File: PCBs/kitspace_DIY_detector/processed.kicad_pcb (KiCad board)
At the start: 2 copper layers, 75 x 26 mm, 35 parts, among them J1 Conn_01x02_Female, J2 Conn_01x02_Female, U1 TLE2072

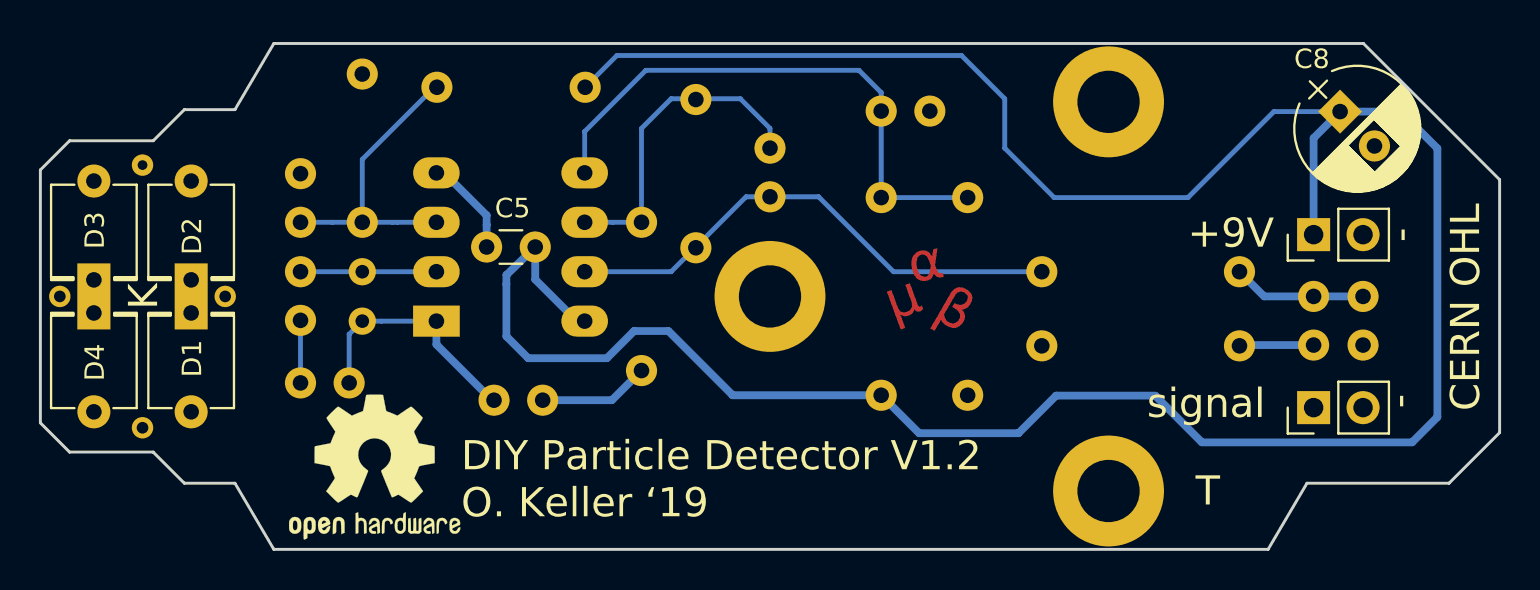
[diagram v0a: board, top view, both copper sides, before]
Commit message: recheck all circuits and clean up fill zone by rerouting the nets using freerouting and manually
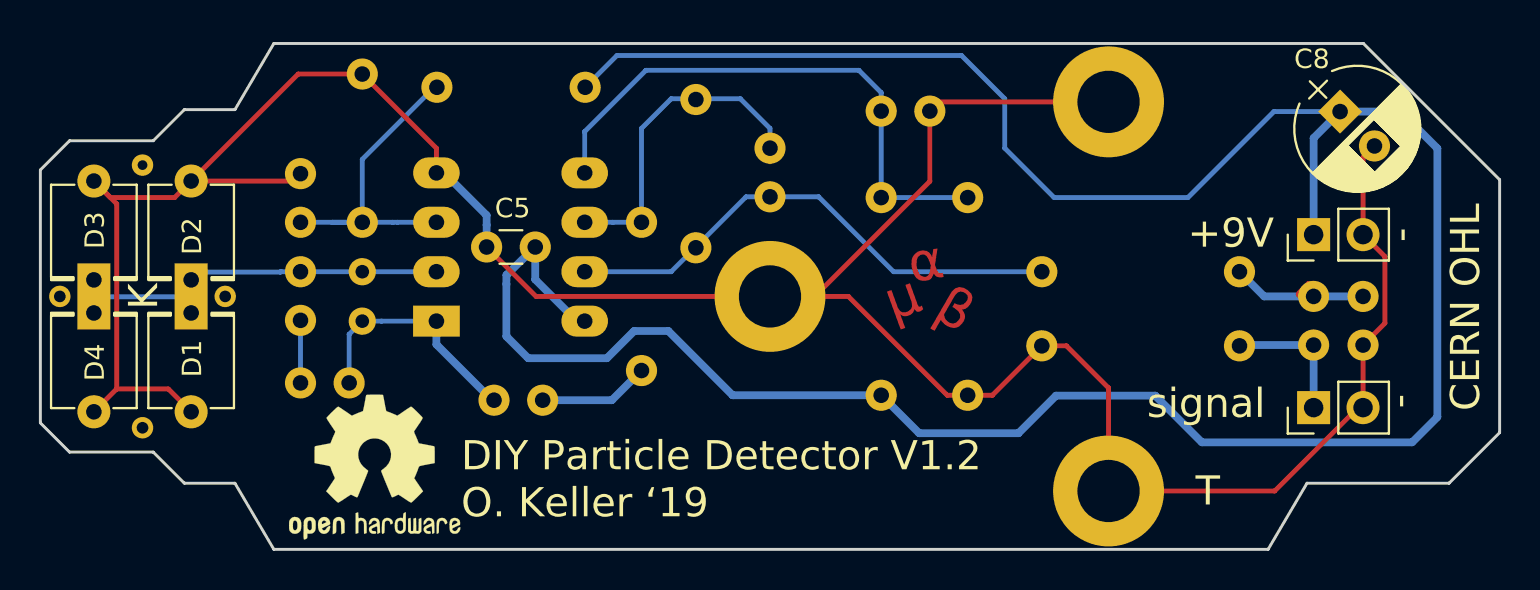
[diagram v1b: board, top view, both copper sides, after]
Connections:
- C3 pad 2: (no net) -> GND
- C7 pad 2: (no net) -> GND
- C8 pad 2: (no net) -> GND
- C9 pad 2: (no net) -> GND
- D1 pad 1: (no net) -> Net-(C1-Pad1)
- D1 pad 2: (no net) -> GND
- D2 pad 1: (no net) -> Net-(C1-Pad1)
- D2 pad 2: (no net) -> GND
- D3 pad 1: (no net) -> Net-(C1-Pad1)
- D3 pad 2: (no net) -> GND
- D4 pad 1: (no net) -> Net-(C1-Pad1)
- D4 pad 2: (no net) -> GND
- J1 pad 2: (no net) -> GND
- J2 pad 1: (no net) -> /Output
- J2 pad 2: (no net) -> GND
- MK5 pad 1: (no net) -> GND
- MK6 pad 1: (no net) -> GND
- MK7 pad 1: (no net) -> GND
- R2 pad 2: (no net) -> GND
- R5 pad 1: (no net) -> Net-(C6-Pad2)
- R5 pad 2: (no net) -> Net-(C6-Pad1)
- R7 pad 2: (no net) -> GND
- R9 pad 2: (no net) -> GND
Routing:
- net GND: track 5.11 -> 148.1 mm
- net Net-(C1-Pad1): track 6.98 -> 22.6 mm
- net /Output: track 3.83 -> 7.32 mm
- net Net-(C3-Pad1): track 15.6 -> 17.3 mm
- net Net-(C10-Pad1): track 6.88 -> 7.80 mm
- net Net-(C6-Pad1): track 16.6 -> 17.2 mm

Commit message: clean psbc that are missed before
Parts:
- renumbered REF*** to REF***_2
